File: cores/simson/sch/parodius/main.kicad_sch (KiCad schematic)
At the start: 23 parts

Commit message: issue #517 done
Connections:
- net VCC: now also G7.16 (VCC)
- net VSS: now also G7.8 (VSS); no longer F5.16 (GND), H5.16 (GND), PAL1.10 (GND)
- net RESET renamed ~{RESET}
- new net GND: F5.16 (GND), H5.16 (GND), PAL1.10 (GND)
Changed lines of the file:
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@@
   (junction (at 335.28 100.33) (diameter 0) (color 0 0 0 0)
   )
+  (junction (at 179.07 130.81) (diameter 0) (color 0 0 0 0)
+  )
   (junction (at 347.98 100.33) (diameter 0) (color 0 0 0 0)
   )
@@
   (junction (at 370.84 100.33) (diameter 0) (color 0 0 0 0)
   )
+  (junction (at 186.69 130.81) (diameter 0) (color 0 0 0 0)
+  )
   (junction (at 363.22 64.77) (diameter 0) (color 0 0 0 0)
   )
@@
     (stroke (width 0) (type default))
   )
-  (wire (pts (xy 288.29 212.09) (xy 275.59 212.09))
+  (wire (pts (xy 278.13 212.09) (xy 275.59 212.09))
     (stroke (width 0) (type default))
   )
@@
     (stroke (width 0) (type default))
   )
+  (wire (pts (xy 186.69 130.81) (xy 191.77 130.81))
+    (stroke (width 0) (type default))
+  )
   (wire (pts (xy 198.12 44.45) (xy 199.39 44.45))
     (stroke (width 0) (type default))
@@
     (stroke (width 0) (type default))
   )
-  (wire (pts (xy 179.07 130.81) (xy 191.77 130.81))
+  (wire (pts (xy 179.07 130.81) (xy 186.69 130.81))
     (stroke (width 0) (type default))
   )
@@
     (effects (font (size 1.27 1.27)) (justify left bottom))
   )
+  (label "GND" (at 262.89 123.19 180) (fields_autoplaced)
+    (effects (font (size 1.27 1.27)) (justify right bottom))
+  )
   (label "BANK~{CS}" (at 43.18 224.79 0) (fields_autoplaced)
     (effects (font (size 1.27 1.27)) (justify left bottom))
@@
     (effects (font (size 1.27 1.27)) (justify left bottom))
   )
-  (label "~{OUTCS}" (at 288.29 212.09 180) (fields_autoplaced)
-    (effects (font (size 1.27 1.27)) (justify right bottom))
-  )
   (label "MAIN_D0" (at 162.56 77.47 0) (fields_autoplaced)
     (effects (font (size 1.27 1.27)) (justify left bottom))
@@
     (effects (font (size 1.27 1.27)) (justify right bottom))
   )
-  (label "VSS" (at 198.12 219.71 180) (fields_autoplaced)
+  (label "GND" (at 198.12 219.71 180) (fields_autoplaced)
     (effects (font (size 1.27 1.27)) (justify right bottom))
   )
@@
     (effects (font (size 1.27 1.27)) (justify left bottom))
   )
-  (label "VSS" (at 262.89 203.2 180) (fields_autoplaced)
-    (effects (font (size 1.27 1.27)) (justify right bottom))
-  )
   (label "MAIN_A16" (at 228.6 100.33 180) (fields_autoplaced)
     (effects (font (size 1.27 1.27)) (justify right bottom))
@@
     (effects (font (size 1.27 1.27)) (justify left bottom))
   )
+  (label "GND" (at 262.89 203.2 180) (fields_autoplaced)
+    (effects (font (size 1.27 1.27)) (justify right bottom))
+  )
   (label "MAIN_A13" (at 104.14 189.23 0) (fields_autoplaced)
     (effects (font (size 1.27 1.27)) (justify left bottom))
@@
     (effects (font (size 1.27 1.27)) (justify left))
   )
-  (hierarchical_label "RESET" (shape input) (at 50.8 173.99 180) (fields_autoplaced)
+  (hierarchical_label "~{RESET}" (shape input) (at 50.8 173.99 180) (fields_autoplaced)
     (effects (font (size 1.27 1.27)) (justify right))
   )
+  (hierarchical_label "~{OUTCS}" (shape output) (at 278.13 212.09 0) (fields_autoplaced)
+    (effects (font (size 1.27 1.27)) (justify left))
+  )
   (hierarchical_label "PAL_BANK" (shape output) (at 82.55 212.09 0) (fields_autoplaced)
     (effects (font (size 1.27 1.27)) (justify left))
@@
     (effects (font (size 1.27 1.27)) (justify left))
   )
-  (hierarchical_label "RESET" (shape input) (at 49.53 229.87 180) (fields_autoplaced)
+  (hierarchical_label "~{RESET}" (shape input) (at 49.53 229.87 180) (fields_autoplaced)
     (effects (font (size 1.27 1.27)) (justify right))
   )
@@
     (effects (font (size 1.27 1.27)) (justify right))
   )
-  (hierarchical_label "RESET" (shape input) (at 95.25 123.19 180) (fields_autoplaced)
+  (hierarchical_label "~{RESET}" (shape input) (at 95.25 123.19 180) (fields_autoplaced)
     (effects (font (size 1.27 1.27)) (justify right))
   )
@@
     )
   )
+  (symbol (lib_id "power:PWR_FLAG") (at 198.12 219.71 180) (unit 1)
+    (in_bom yes) (on_board yes) (dnp no)
+    (property "Reference" "#FLG042" (at 198.12 221.615 0)
+      (effects (font (size 1.27 1.27)) hide)
+    )
+    (property "Value" "PWR_FLAG" (at 198.12 223.52 0)
+      (effects (font (size 1.27 1.27)))
+    )
+    (property "Footprint" "" (at 198.12 219.71 0)
+      (effects (font (size 1.27 1.27)) hide)
+    )
+    (property "Datasheet" "~" (at 198.12 219.71 0)
+      (effects (font (size 1.27 1.27)) hide)
+    )
+    (pin "1")
+    (instances
+      (project "paroda"
+        (path "/0011ec10-82c4-4039-b424-337480f568e8/7d4ab3ba-37fa-4111-bbdb-c99f1a708a52"
+          (reference "#FLG042") (unit 1)
+        )
+      )
+    )
+  )
   (symbol (lib_id "jt74:74LS139") (at 262.89 214.63 0) (unit 2)
     (in_bom yes) (on_board yes) (dnp no)
@@
     )
   )
+  (symbol (lib_id "power:VSS") (at 179.07 130.81 180) (unit 1)
+    (in_bom yes) (on_board yes) (dnp no)
+    (property "Reference" "#PWR042" (at 179.07 127 0)
+      (effects (font (size 1.27 1.27)) hide)
+    )
+    (property "Value" "VSS" (at 179.07 134.62 0)
+      (effects (font (size 1.27 1.27)))
+    )
+    (property "Footprint" "" (at 179.07 130.81 0)
+      (effects (font (size 1.27 1.27)) hide)
+    )
+    (property "Datasheet" "" (at 179.07 130.81 0)
+      (effects (font (size 1.27 1.27)) hide)
+    )
+    (pin "1")
+    (instances
+      (project "paroda"
+        (path "/0011ec10-82c4-4039-b424-337480f568e8/7d4ab3ba-37fa-4111-bbdb-c99f1a708a52"
+          (reference "#PWR042") (unit 1)
+        )
+      )
+    )
+  )
   (symbol (lib_id "jt74:74LS74") (at 99.06 40.64 0) (unit 1)
     (in_bom yes) (on_board yes) (dnp no)
@@
     )
   )
-  (symbol (lib_id "power:VSS") (at 262.89 123.19 180) (unit 1)
-    (in_bom yes) (on_board yes) (dnp no)
-    (property "Reference" "#PWR0102" (at 262.89 119.38 0)
-      (effects (font (size 1.27 1.27)) hide)
-    )
-    (property "Value" "VSS" (at 262.89 127 0)
-      (effects (font (size 1.27 1.27)))
-    )
-    (property "Footprint" "" (at 262.89 123.19 0)
-      (effects (font (size 1.27 1.27)) hide)
-    )
-    (property "Datasheet" "" (at 262.89 123.19 0)
-      (effects (font (size 1.27 1.27)) hide)
-    )
-    (pin "1")
-    (instances
-      (project "paroda"
-        (path "/0011ec10-82c4-4039-b424-337480f568e8/7d4ab3ba-37fa-4111-bbdb-c99f1a708a52"
-          (reference "#PWR0102") (unit 1)
-        )
-      )
-    )
-  )
   (symbol (lib_id "konami:053248") (at 198.12 87.63 0) (unit 1)
     (in_bom yes) (on_board yes) (dnp no)
@@
     )
   )
+  (symbol (lib_id "power:PWR_FLAG") (at 186.69 130.81 180) (unit 1)
+    (in_bom yes) (on_board yes) (dnp no)
+    (property "Reference" "#FLG043" (at 186.69 132.715 0)
+      (effects (font (size 1.27 1.27)) hide)
+    )
+    (property "Value" "PWR_FLAG" (at 186.69 134.62 0)
+      (effects (font (size 1.27 1.27)))
+    )
+    (property "Footprint" "" (at 186.69 130.81 0)
+      (effects (font (size 1.27 1.27)) hide)
+    )
+    (property "Datasheet" "~" (at 186.69 130.81 0)
+      (effects (font (size 1.27 1.27)) hide)
+    )
+    (pin "1")
+    (instances
+      (project "paroda"
+        (path "/0011ec10-82c4-4039-b424-337480f568e8/7d4ab3ba-37fa-4111-bbdb-c99f1a708a52"
+          (reference "#FLG043") (unit 1)
+        )
+      )
+    )
+  )
   (symbol (lib_id "jt74:74LS04") (at 231.14 275.59 0) (unit 2)
     (in_bom yes) (on_board yes) (dnp no)
@@
     (pin "7")
     (pin "9")
+    (pin "16")
+    (pin "8")
     (instances
       (project "paroda"

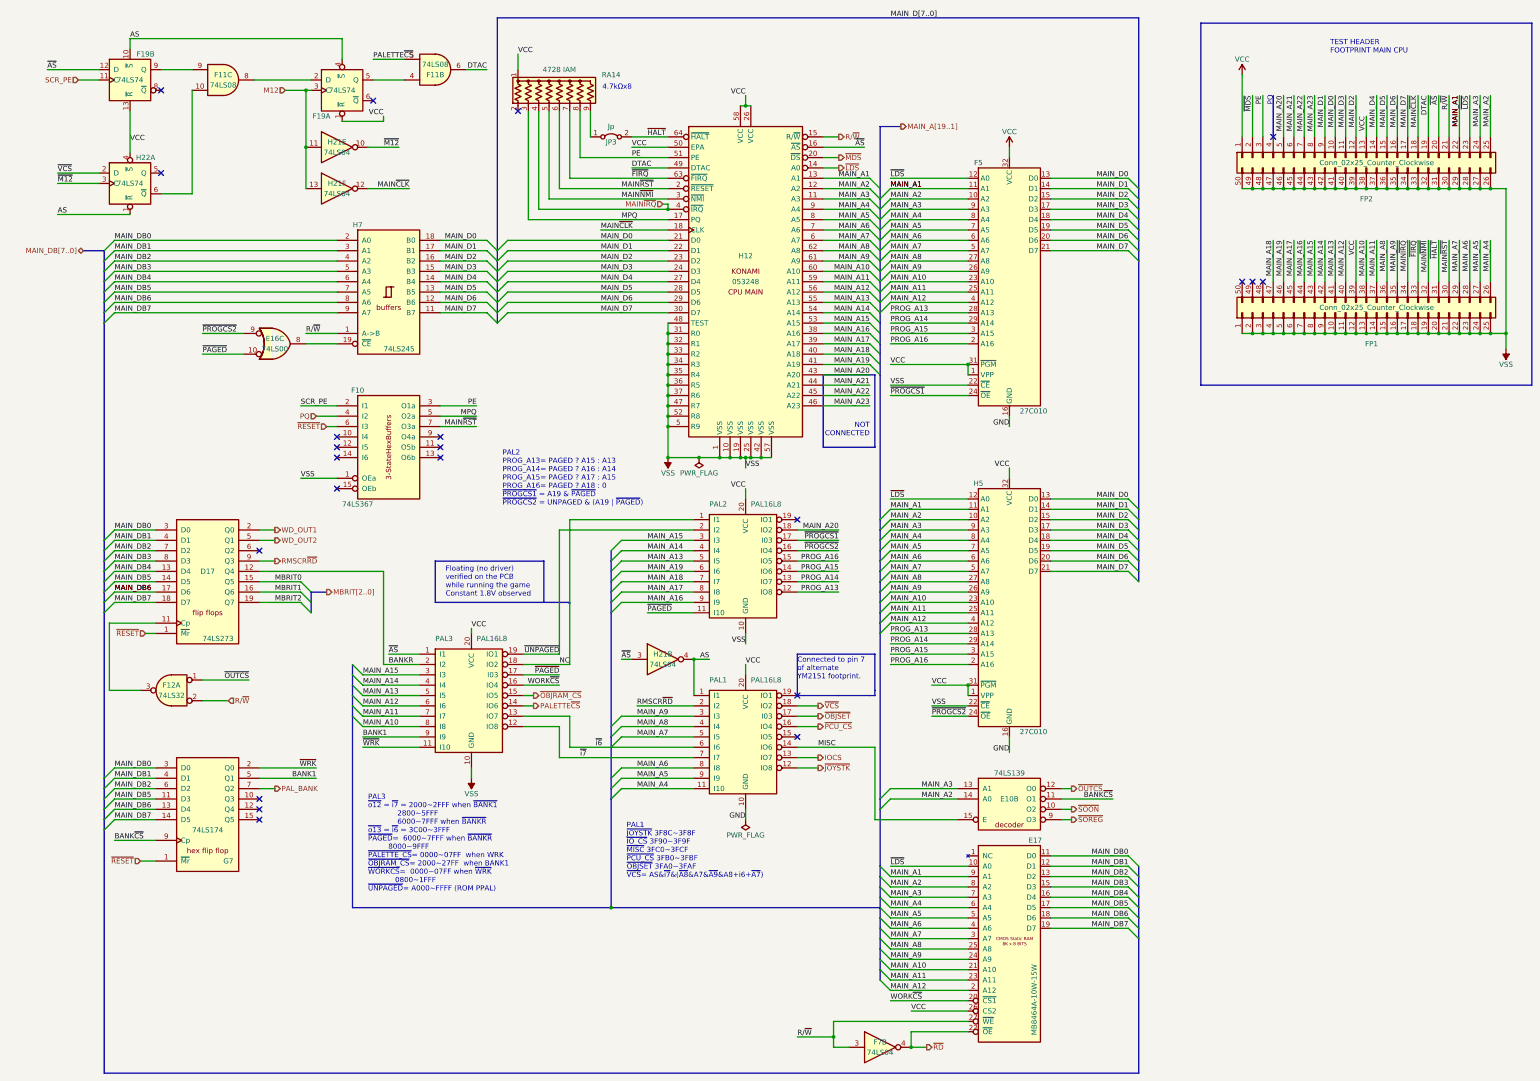
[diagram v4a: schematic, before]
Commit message: issue #537 parodius
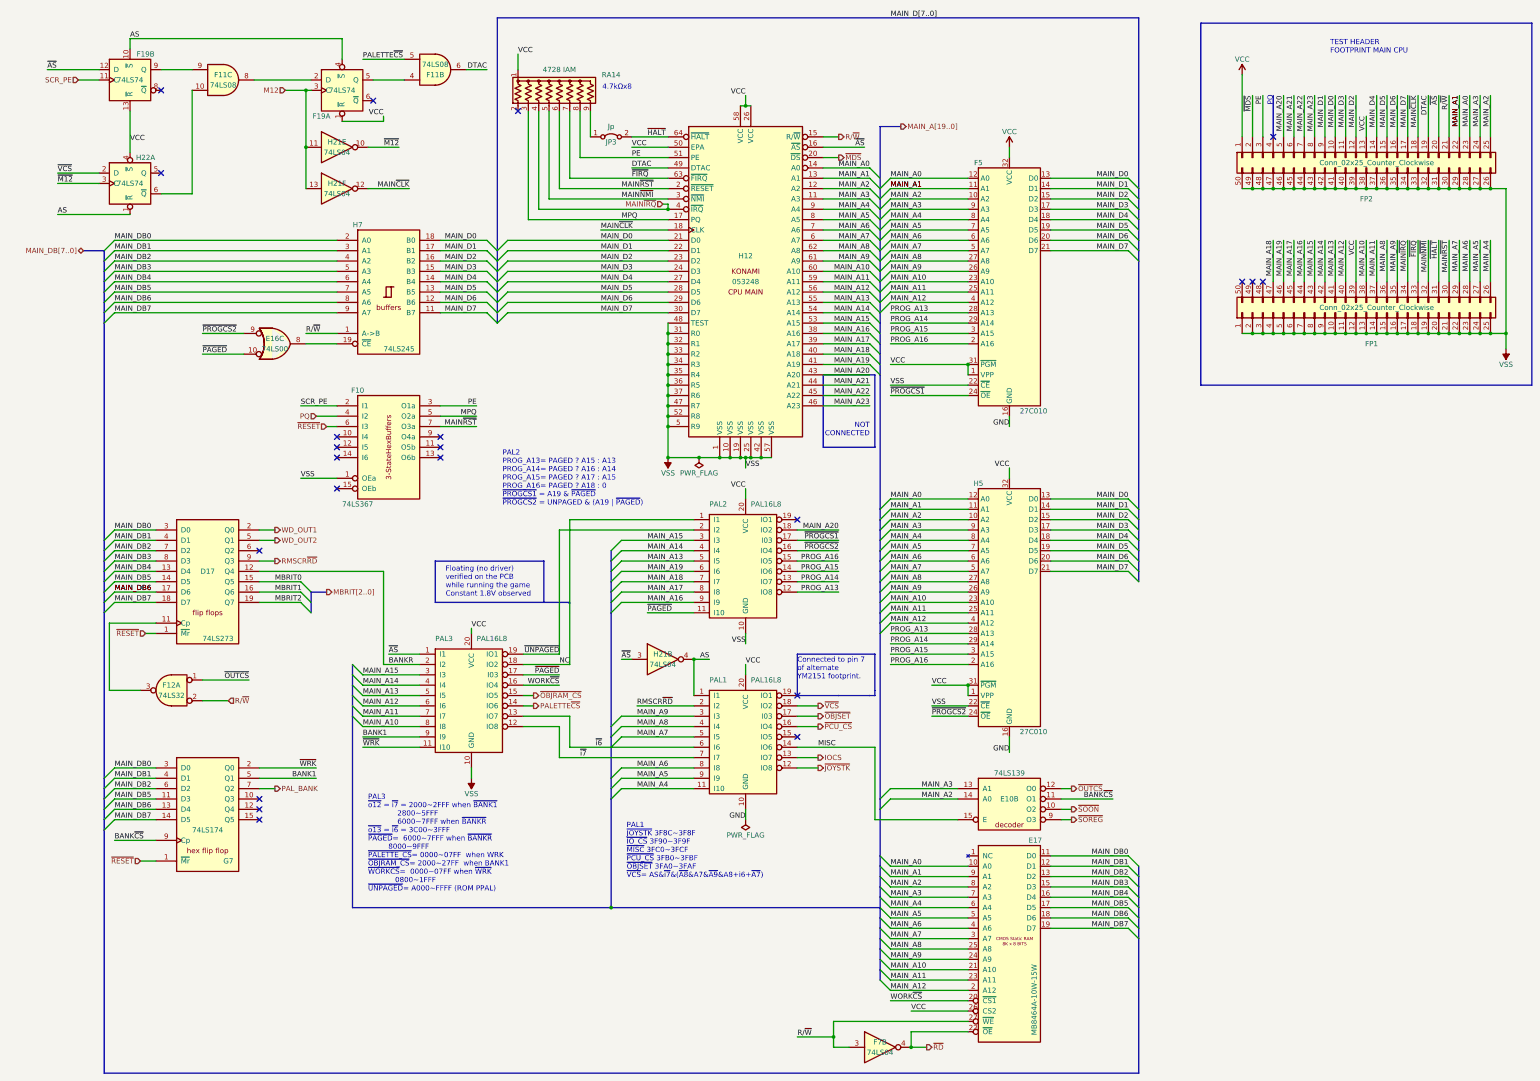
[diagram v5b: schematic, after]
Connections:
- net ~{LDS} renamed MAIN_A0
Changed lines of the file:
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@@
     (stroke (width 0) (type default))
   )
+  (bus_entry (at 231.14 64.77) (size 2.54 -2.54)
+    (stroke (width 0) (type default))
+  )
   (bus_entry (at 228.6 100.33) (size 2.54 2.54)
     (stroke (width 0) (type default))
@@
     (stroke (width 0) (type default))
   )
+  (bus_entry (at 231.14 143.51) (size 2.54 -2.54)
+    (stroke (width 0) (type default))
+  )
   (bus_entry (at 231.14 148.59) (size 2.54 -2.54)
     (stroke (width 0) (type default))
@@
     (stroke (width 0) (type default))
   )
+  (bus_entry (at 228.6 59.69) (size 2.54 2.54)
+    (stroke (width 0) (type default))
+  )
   (bus_entry (at 228.6 92.71) (size 2.54 2.54)
     (stroke (width 0) (type default))
@@
     (stroke (width 0) (type default))
   )
+  (bus_entry (at 231.14 228.6) (size 2.54 2.54)
+    (stroke (width 0) (type default))
+  )
   (bus_entry (at 231.14 233.68) (size 2.54 2.54)
     (stroke (width 0) (type default))
@@
     (stroke (width 0) (type default))
   )
-  (bus (pts (xy 231.14 217.17) (xy 231.14 231.14))
+  (bus (pts (xy 231.14 217.17) (xy 231.14 228.6))
     (stroke (width 0) (type default))
   )
-  (bus (pts (xy 231.14 110.49) (xy 231.14 146.05))
+  (bus (pts (xy 231.14 110.49) (xy 231.14 143.51))
     (stroke (width 0) (type default))
   )
@@
     (stroke (width 0) (type default))
   )
-  (wire (pts (xy 217.17 59.69) (xy 220.98 59.69))
+  (wire (pts (xy 217.17 59.69) (xy 228.6 59.69))
     (stroke (width 0) (type default))
   )
@@
     (stroke (width 0) (type default))
   )
+  (bus (pts (xy 231.14 228.6) (xy 231.14 231.14))
+    (stroke (width 0) (type default))
+  )
   (wire (pts (xy 62.23 40.64) (xy 62.23 66.04))
     (stroke (width 0) (type default))
@@
     (stroke (width 0) (type default))
   )
-  (bus (pts (xy 231.14 49.53) (xy 231.14 64.77))
+  (bus (pts (xy 231.14 49.53) (xy 231.14 62.23))
     (stroke (width 0) (type default))
   )
@@
     (stroke (width 0) (type default))
   )
-  (wire (pts (xy 106.68 33.02) (xy 114.3 33.02))
+  (wire (pts (xy 104.14 33.02) (xy 114.3 33.02))
     (stroke (width 0) (type default))
   )
@@
     (stroke (width 0) (type default))
   )
+  (bus (pts (xy 231.14 62.23) (xy 231.14 64.77))
+    (stroke (width 0) (type default))
+  )
   (wire (pts (xy 82.55 151.13) (xy 78.74 151.13))
     (stroke (width 0) (type default))
@@
     (stroke (width 0) (type default))
   )
+  (bus (pts (xy 231.14 143.51) (xy 231.14 146.05))
+    (stroke (width 0) (type default))
+  )
   (wire (pts (xy 252.73 168.91) (xy 233.68 168.91))
     (stroke (width 0) (type default))
@@
     (effects (font (size 1.27 1.27)) (justify left bottom))
   )
-  (label "~{LDS}" (at 233.68 62.23 0) (fields_autoplaced)
+  (label "MAIN_A0" (at 233.68 62.23 0) (fields_autoplaced)
     (effects (font (size 1.27 1.27)) (justify left bottom))
   )
@@
     (effects (font (size 1.27 1.27)) (justify right bottom))
   )
+  (label "MAIN_A0" (at 228.6 59.69 180) (fields_autoplaced)
+    (effects (font (size 1.27 1.27)) (justify right bottom))
+  )
   (label "VCC" (at 347.98 77.47 270) (fields_autoplaced)
     (effects (font (size 1.27 1.27)) (justify right bottom))
@@
     (effects (font (size 1.27 1.27)) (justify right bottom))
   )
-  (label "~{LDS}" (at 233.68 231.14 0) (fields_autoplaced)
+  (label "MAIN_A0" (at 233.68 231.14 0) (fields_autoplaced)
     (effects (font (size 1.27 1.27)) (justify left bottom))
   )
@@
     (effects (font (size 1.27 1.27)) (justify left bottom))
   )
-  (label "~{LDS}" (at 375.92 41.91 270) (fields_autoplaced)
+  (label "MAIN_A0" (at 375.92 41.91 270) (fields_autoplaced)
     (effects (font (size 1.27 1.27)) (justify right bottom))
   )
@@
     (effects (font (size 1.27 1.27)) (justify left bottom))
   )
-  (label "~{LDS}" (at 233.68 140.97 0) (fields_autoplaced)
+  (label "MAIN_A0" (at 233.68 140.97 0) (fields_autoplaced)
     (effects (font (size 1.27 1.27)) (justify left bottom))
   )
@@
     (effects (font (size 1.27 1.27)) (justify right bottom))
   )
-  (label "PALETTE~{CS}" (at 106.68 33.02 0) (fields_autoplaced)
+  (label "PALETTE~{CS}" (at 104.14 33.02 0) (fields_autoplaced)
     (effects (font (size 1.27 1.27)) (justify left bottom))
   )
@@
     (effects (font (size 1.27 1.27)) (justify right))
   )
-  (hierarchical_label "~{LDS}" (shape output) (at 220.98 59.69 0) (fields_autoplaced)
-    (effects (font (size 1.27 1.27)) (justify left))
-  )
   (hierarchical_label "~{PCU_CS}" (shape output) (at 215.9 196.85 0) (fields_autoplaced)
     (effects (font (size 1.27 1.27)) (justify left))
@@
     (effects (font (size 1.27 1.27)) (justify left))
   )
-  (hierarchical_label "MAIN_A[19..1]" (shape output) (at 236.22 49.53 0) (fields_autoplaced)
+  (hierarchical_label "MAIN_A[19..0]" (shape output) (at 236.22 49.53 0) (fields_autoplaced)
     (effects (font (size 1.27 1.27)) (justify left))
   )

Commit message: sch: changed copyright notice
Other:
- company: Esperanza Triana -> JOTEGO
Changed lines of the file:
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@@
     (date "2023-05-09")
     (rev "José Tejada G.")
-    (company "Esperanza Triana")
+    (company "JOTEGO")
     (comment 1 "www.patreon.com/jotego")
     (comment 2 "JOTEGO")
